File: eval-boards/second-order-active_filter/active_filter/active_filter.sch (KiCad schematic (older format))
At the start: 24 parts, among them J1 IN_A, J2 IN_B, J3 Conn_01x03_Male, J4 OUT_A, J5 OUT_B, U1 ADA4075-2

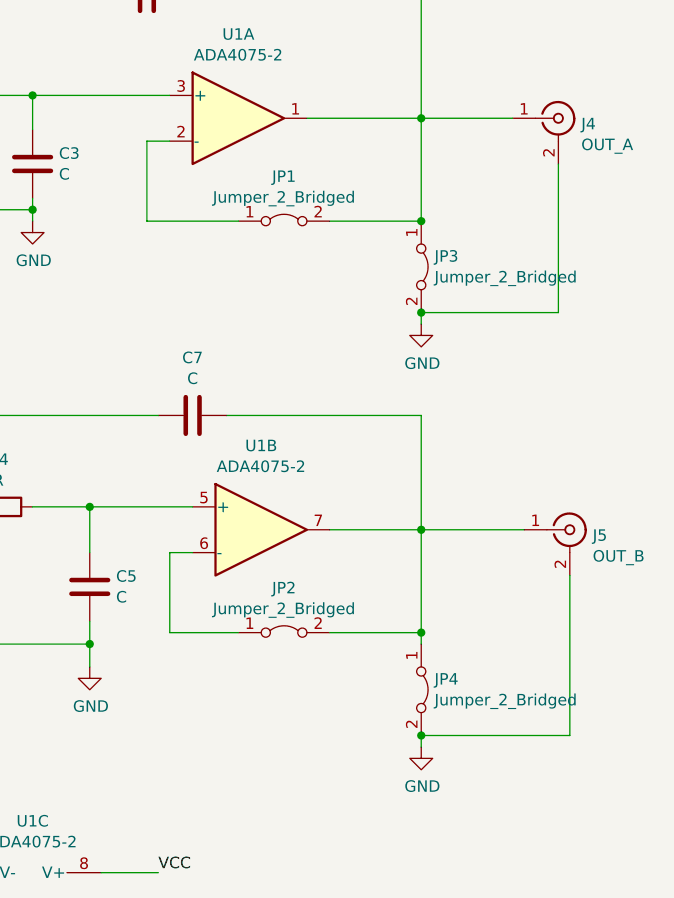
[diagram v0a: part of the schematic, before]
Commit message: power_and_RF_updated
修正了ADA4817和有源滤波器的电源线管脚、反馈电阻和焊盘handsold
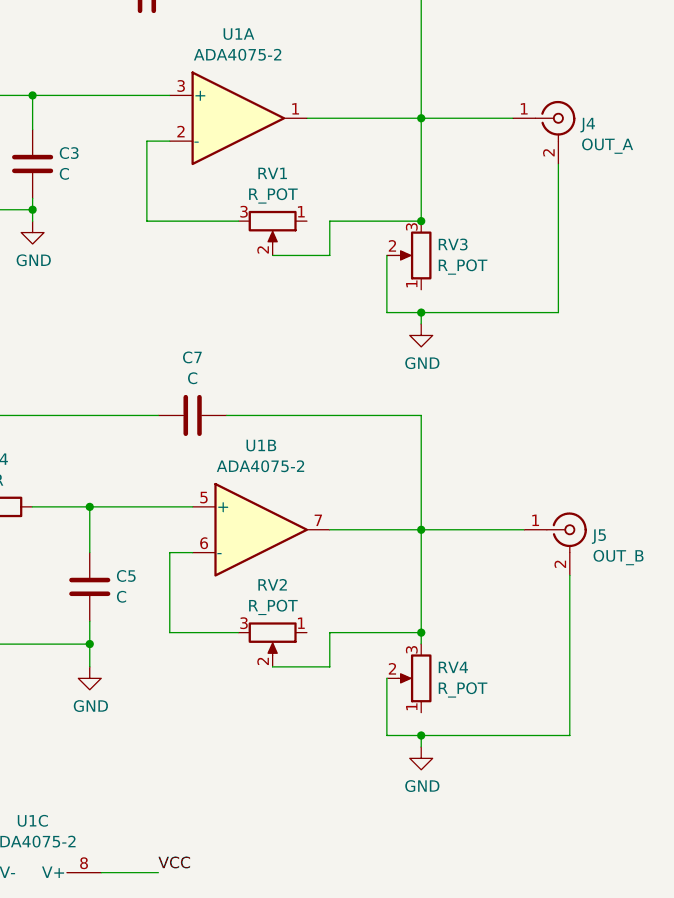
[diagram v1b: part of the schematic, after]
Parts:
- removed JP1, JP2, JP3, JP4: Jumper_2_Bridged, Jumper:SolderJumper-2_P1.3mm_Open_TrianglePad1.0x1.5mm, symbol Jumper:Jumper_2_Bridged
- added RV1, RV2, RV3, RV4: R_POT, Connector_PinSocket_2.54mm:PinSocket_1x03_P2.54mm_Vertical, symbol Device:R_POT
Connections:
- net GND: now also RV3.2, RV4.2
- net at C6.1, J4.1 (In), U1.1: now also RV1.2, RV3.3
- net at U1.2 (-): now also RV1.3
- net at U1.6 (-): now also RV2.3
- net at C7.1, J5.1 (In), U1.7: now also RV2.2, RV4.3
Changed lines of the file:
@@
 EESchema Schematic File Version 4
+LIBS:active_filter-cache
 EELAYER 29 0
 EELAYER END
@@
 $EndDescr
 $Comp
-L Amplifier_Operational:ADA4075-2 U1
-U 1 1 5D204576
-P 6000 1950
-F 0 "U1" H 6000 2317 50  0000 C CNN
-F 1 "ADA4075-2" H 6000 2226 50  0000 C CNN
-F 2 "Package_SO:SOIC-8_3.9x4.9mm_P1.27mm" H 6000 1950 50  0001 C CNN
-F 3 "https://www.analog.com/static/imported-files/data_sheets/ADA4075-2.pdf" H 6000 1950 50  0001 C CNN
-	1    6000 1950
-	1    0    0    -1
-$EndComp
-$Comp
 L Device:C C3
 U 1 1 5D205F37
@@
 	5750 1400 6800 1400
 Wire Wire Line
-	6800 1400 6800 1950
-Wire Wire Line
-	6800 1950 6300 1950
-Wire Wire Line
 	5700 2050 5600 2050
 Wire Wire Line
@@
 Wire Wire Line
 	5600 2400 6000 2400
-Wire Wire Line
-	6800 2400 6800 1950
-Connection ~ 6800 1950
 Wire Wire Line
 	5100 2000 5100 1850
@@
 Connection ~ 6800 3750
 Wire Wire Line
-	6800 1950 7200 1950
-$Comp
-L Jumper:Jumper_2_Bridged JP2
-U 1 1 5D227BFD
-P 6200 4200
-F 0 "JP2" H 6200 4395 50  0000 C CNN
-F 1 "Jumper_2_Bridged" H 6200 4304 50  0000 C CNN
-F 2 "Jumper:SolderJumper-2_P1.3mm_Open_TrianglePad1.0x1.5mm" H 6200 4200 50  0001 C CNN
-F 3 "~" H 6200 4200 50  0001 C CNN
-	1    6200 4200
-	1    0    0    -1
-$EndComp
-Wire Wire Line
 	6400 4200 6800 4200
-$Comp
-L Jumper:Jumper_2_Bridged JP4
-U 1 1 5D228967
-P 6800 4450
-F 0 "JP4" V 6754 4508 50  0000 L CNN
-F 1 "Jumper_2_Bridged" V 6845 4508 50  0000 L CNN
-F 2 "Jumper:SolderJumper-2_P1.3mm_Open_TrianglePad1.0x1.5mm" H 6800 4450 50  0001 C CNN
-F 3 "~" H 6800 4450 50  0001 C CNN
-	1    6800 4450
-	0    1    1    0
-$EndComp
 $Comp
 L power:GND #PWR04
@@
 	6800 4250 6800 4200
 Connection ~ 6800 4200
-$Comp
-L Jumper:Jumper_2_Bridged JP1
-U 1 1 5D22E215
-P 6200 2400
-F 0 "JP1" H 6200 2595 50  0000 C CNN
-F 1 "Jumper_2_Bridged" H 6200 2504 50  0000 C CNN
-F 2 "Jumper:SolderJumper-2_P1.3mm_Open_TrianglePad1.0x1.5mm" H 6200 2400 50  0001 C CNN
-F 3 "~" H 6200 2400 50  0001 C CNN
-	1    6200 2400
-	1    0    0    -1
-$EndComp
-Wire Wire Line
-	6400 2400 6800 2400
 Wire Wire Line
 	4550 3650 4700 3650
-$Comp
-L Jumper:Jumper_2_Bridged JP3
-U 1 1 5D22EFCC
-P 6800 2600
-F 0 "JP3" V 6754 2658 50  0000 L CNN
-F 1 "Jumper_2_Bridged" V 6845 2658 50  0000 L CNN
-F 2 "Jumper:SolderJumper-2_P1.3mm_Open_TrianglePad1.0x1.5mm" H 6800 2600 50  0001 C CNN
-F 3 "~" H 6800 2600 50  0001 C CNN
-	1    6800 2600
-	0    1    1    0
-$EndComp
 Wire Wire Line
 	6800 3250 6800 3750
@@
 Wire Wire Line
 	4700 3650 4800 3650
-Connection ~ 6800 2400
 $Comp
 L power:GND #PWR03
@@
 Wire Wire Line
 	7450 4650 6800 4650
-Connection ~ 6800 4650
 Wire Wire Line
 	3650 3850 3650 4250
@@
 Wire Wire Line
 	5100 2350 5100 2300
-Wire Wire Line
-	6800 2850 6800 2800
-Wire Wire Line
-	7400 2150 7400 2800
-Wire Wire Line
-	7400 2800 6800 2800
-Connection ~ 6800 2800
 Wire Wire Line
 	4950 5800 4800 5800
@@
 Text Label 5650 5250 0    50   ~ 0
 VCC
+$Comp
+L Device:R_POT RV2
+U 1 1 5D26EB7B
+P 6150 4200
+F 0 "RV2" V 5943 4200 50  0000 C CNN
+F 1 "R_POT" V 6034 4200 50  0000 C CNN
+F 2 "Connector_PinSocket_2.54mm:PinSocket_1x03_P2.54mm_Vertical" H 6150 4200 50  0001 C CNN
+F 3 "~" H 6150 4200 50  0001 C CNN
+	1    6150 4200
+	0    1    1    0
+$EndComp
+$Comp
+L Device:R_POT RV4
+U 1 1 5D26EECE
+P 6800 4400
+F 0 "RV4" H 6730 4354 50  0000 R CNN
+F 1 "R_POT" H 6730 4445 50  0000 R CNN
+F 2 "Connector_PinSocket_2.54mm:PinSocket_1x03_P2.54mm_Vertical" H 6800 4400 50  0001 C CNN
+F 3 "~" H 6800 4400 50  0001 C CNN
+	1    6800 4400
+	-1   0    0    1
+$EndComp
+Wire Wire Line
+	6650 4400 6650 4650
+Wire Wire Line
+	6650 4650 6800 4650
+Connection ~ 6800 4650
+Wire Wire Line
+	6150 4350 6400 4350
+Wire Wire Line
+	6400 4350 6400 4200
+Wire Wire Line
+	7400 2150 7400 2800
+Connection ~ 6800 2800
+Wire Wire Line
+	6650 2800 6800 2800
+Wire Wire Line
+	6650 2550 6650 2800
+Connection ~ 6800 2400
+$Comp
+L Device:R_POT RV3
+U 1 1 5D26BC6B
+P 6800 2550
+F 0 "RV3" H 6730 2504 50  0000 R CNN
+F 1 "R_POT" H 6730 2595 50  0000 R CNN
+F 2 "Connector_PinSocket_2.54mm:PinSocket_1x03_P2.54mm_Vertical" H 6800 2550 50  0001 C CNN
+F 3 "~" H 6800 2550 50  0001 C CNN
+	1    6800 2550
+	-1   0    0    1
+$EndComp
+Wire Wire Line
+	6400 2550 6400 2400
+Wire Wire Line
+	6150 2550 6400 2550
+$Comp
+L Device:R_POT RV1
+U 1 1 5D268119
+P 6150 2400
+F 0 "RV1" V 5943 2400 50  0000 C CNN
+F 1 "R_POT" V 6034 2400 50  0000 C CNN
+F 2 "Connector_PinSocket_2.54mm:PinSocket_1x03_P2.54mm_Vertical" H 6150 2400 50  0001 C CNN
+F 3 "~" H 6150 2400 50  0001 C CNN
+	1    6150 2400
+	0    1    1    0
+$EndComp
+Wire Wire Line
+	7400 2800 6800 2800
+Wire Wire Line
+	6800 2850 6800 2800
+Wire Wire Line
+	6400 2400 6800 2400
+Wire Wire Line
+	6800 1950 7200 1950
+Connection ~ 6800 1950
+Wire Wire Line
+	6800 2400 6800 1950
+Wire Wire Line
+	6800 1950 6300 1950
+Wire Wire Line
+	6800 1400 6800 1950
+$Comp
+L Amplifier_Operational:ADA4075-2 U1
+U 1 1 5D204576
+P 6000 1950
+F 0 "U1" H 6000 2317 50  0000 C CNN
+F 1 "ADA4075-2" H 6000 2226 50  0000 C CNN
+F 2 "Package_SO:SOIC-8_3.9x4.9mm_P1.27mm" H 6000 1950 50  0001 C CNN
+F 3 "https://www.analog.com/static/imported-files/data_sheets/ADA4075-2.pdf" H 6000 1950 50  0001 C CNN
+	1    6000 1950
+	1    0    0    -1
+$EndComp
 $EndSCHEMATC
